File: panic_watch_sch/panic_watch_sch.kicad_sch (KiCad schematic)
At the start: 6 parts, among them IC1 STM32F401RET6, IC2 STM32F401RET6, IC3 STM32F401RET6

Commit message: Semi-finished schematic & config
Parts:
- added BT1: 9V, symbol Device:Battery_Cell
- added D2: IR204A, LED_THT:LED_D3.0mm_IRBlack, symbol LED:IR204A
- added DS2: WC1602A, Display:WC1602A, symbol Display_Character:WC1602A
- added IC4: STM32F401RET6, QFP50P1200X1200X160-64N, symbol STM32F401RET6:STM32F401RET6
- added LS1: Speaker, symbol Device:Speaker
- added PS1: ~, symbol STM32F401RET6:MB102
- added Q1: BC107, Package_TO_SOT_THT:TO-18-3, symbol Transistor_BJT:BC107
- added R1, R2, R3, R4, R5: 1k, symbol Device:R
- added SD1: ~, symbol STM32F401RET6:HW-203
- added U1, U2: TSSP58038, OptoDevice:Vishay_MINICAST-3Pin, symbol Sensor_Proximity:TSSP58038
- added U3: MAX98357A, Package_DFN_QFN:TQFN-16-1EP_3x3mm_P0.5mm_EP1.23x1.23mm, symbol Audio:MAX98357A
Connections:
- net at IC3.45 (PA12): now also U2.1 (OUT)
- net at IC3.47 (VSS_3): now also U2.2 (GND)
- net at IC3.48 (VDD_3): now also R2.2
- net at IC3.58 (PB6): now also IC2.58 (PB6), IC4.58 (PB6)
- net at IC3.59 (PB7): now also IC2.59 (PB7), IC4.57 (PB5)
- net at IC1.10 (PC2): now also DS1.9 (D2)
- net at IC1.11 (PC3): now also DS1.10 (D3)
- net at IC1.12 (VSSA/VREF-): now also U3.11 (GND), U3.15 (GND), U3.3 (GND)
- net Skin1: now reaches IC1.13 (VDDA/VREF+)
- net at IC1.18 (VSS_1): now also R4.1
- net at IC1.20 (PA4): now also U3.14 (LRCLK)
- net at IC1.22 (PA6): now also D1.3 (A), D2.2 (A)
- net at IC1.24 (PC4): now also DS1.11 (D4)
- net at IC1.25 (PC5): now also DS1.12 (D5)
- net at IC1.27 (PB1): now also Q1.1 (E)
- net at IC1.29 (PB10): now also SD1. (SCK)
- net at IC1.31 (VSS_2): now also SD1. (SCK)
- net at IC1.32 (VDD_2): now also SD1. (SCK)
- net at IC1.33 (PB12): now also SD1. (SCK)
- net Skin2: now reaches IC1.34 (PB13)
- net at IC1.35 (PB14): now also SD1. (SCK)
- net at IC1.36 (PB15): now also SD1. (SCK)
- net at IC1.37 (PC6): now also DS1.13 (D6)
- net at IC1.38 (PC7): now also DS1.14 (D7)
- net at IC1.39 (PC8): now also DS1.4 (RS)
- net at IC1.40 (PC9): now also DS1.5 (R/W)
- net at IC1.47 (VSS_3): now also MK1.1 (-)
- net at IC1.48 (VDD_3): now also R3.1
- net at IC1.50 (PA15): now also DS1.3 (VO)
- net at IC1.51 (PC10): now also U3.16 (BCLK)
- net at IC1.53 (PC12): now also U3.1 (DIN)
- net at IC1.54 (PD2): now also DS1.6 (E)
- net at IC1.63 (VSS_4): now also DS1.1 (VSS), DS1.16 (LED(-))
- net at IC1.64 (VDD_4): now also DS1.15 (LED(+))
- net at IC1.8 (PC0): now also DS1.7 (D0)
- net at IC1.9 (PC1): now also DS1.8 (D1)
- net +5V: now reaches DS1.2 (VDD)
- net +5V: now also DS2.2 (VDD), SD1. (SCK), U3.4 (~{SD_MODE}), U3.7 (VDD), U3.8 (VDD)
- net at D1.1 (BK): now also D2.1 (K), R4.2
- net at IC2.10 (PC2): now also DS2.9 (D2)
- net at IC2.11 (PC3): now also DS2.10 (D3)
- net at IC2.24 (PC4): now also DS2.11 (D4)
- net at IC2.25 (PC5): now also DS2.12 (D5)
- net at IC2.37 (PC6): now also DS2.13 (D6)
- net at IC2.38 (PC7): now also DS2.14 (D7)
- net at IC2.39 (PC8): now also DS2.4 (RS)
- net at IC2.40 (PC9): now also DS2.5 (R/W)
- net at IC2.50 (PA15): now also DS2.3 (VO)
- net at IC2.54 (PD2): now also DS2.6 (E)
- net at IC2.63 (VSS_4): now also DS2.1 (VSS), DS2.16 (LED(-))
- net at IC2.64 (VDD_4): now also DS2.15 (LED(+))
- net at IC2.8 (PC0): now also DS2.7 (D0)
- net at IC2.9 (PC1): now also DS2.8 (D1)
- net at MK1.2 (+): now also Q1.2 (B)
- new net: IC4.45 (PA12), U1.1 (OUT)
- new net: IC4.47 (VSS_3), U1.2 (GND)
- new net: R1.1, U1.3 (Vs)
- new net: Q1.3 (C), R3.2
- new net: R2.1, U2.3 (Vs)
- new net: R5.2, U3.2 (GAIN_SLOT)
- new net: IC4.48 (VDD_3), R1.2
- new net: LS1.1, U3.9 (OUTP)
- new net: LS1.2, U3.10 (OUTN)
- new net: BT1.1 (+), PS1. (Vout)
- new net: BT1.2 (-), PS1. (Vout)
- new net E5V: PS1. (Vout)
- new net GND: PS1. (Vout), R5.1
- no-connect marks 0 -> 1
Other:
- removed sheet Receiver and Bus
- removed sheet Wearable Accessory
- moved on the sheet: D1, DS1, IC1, IC2, IC3, MK1

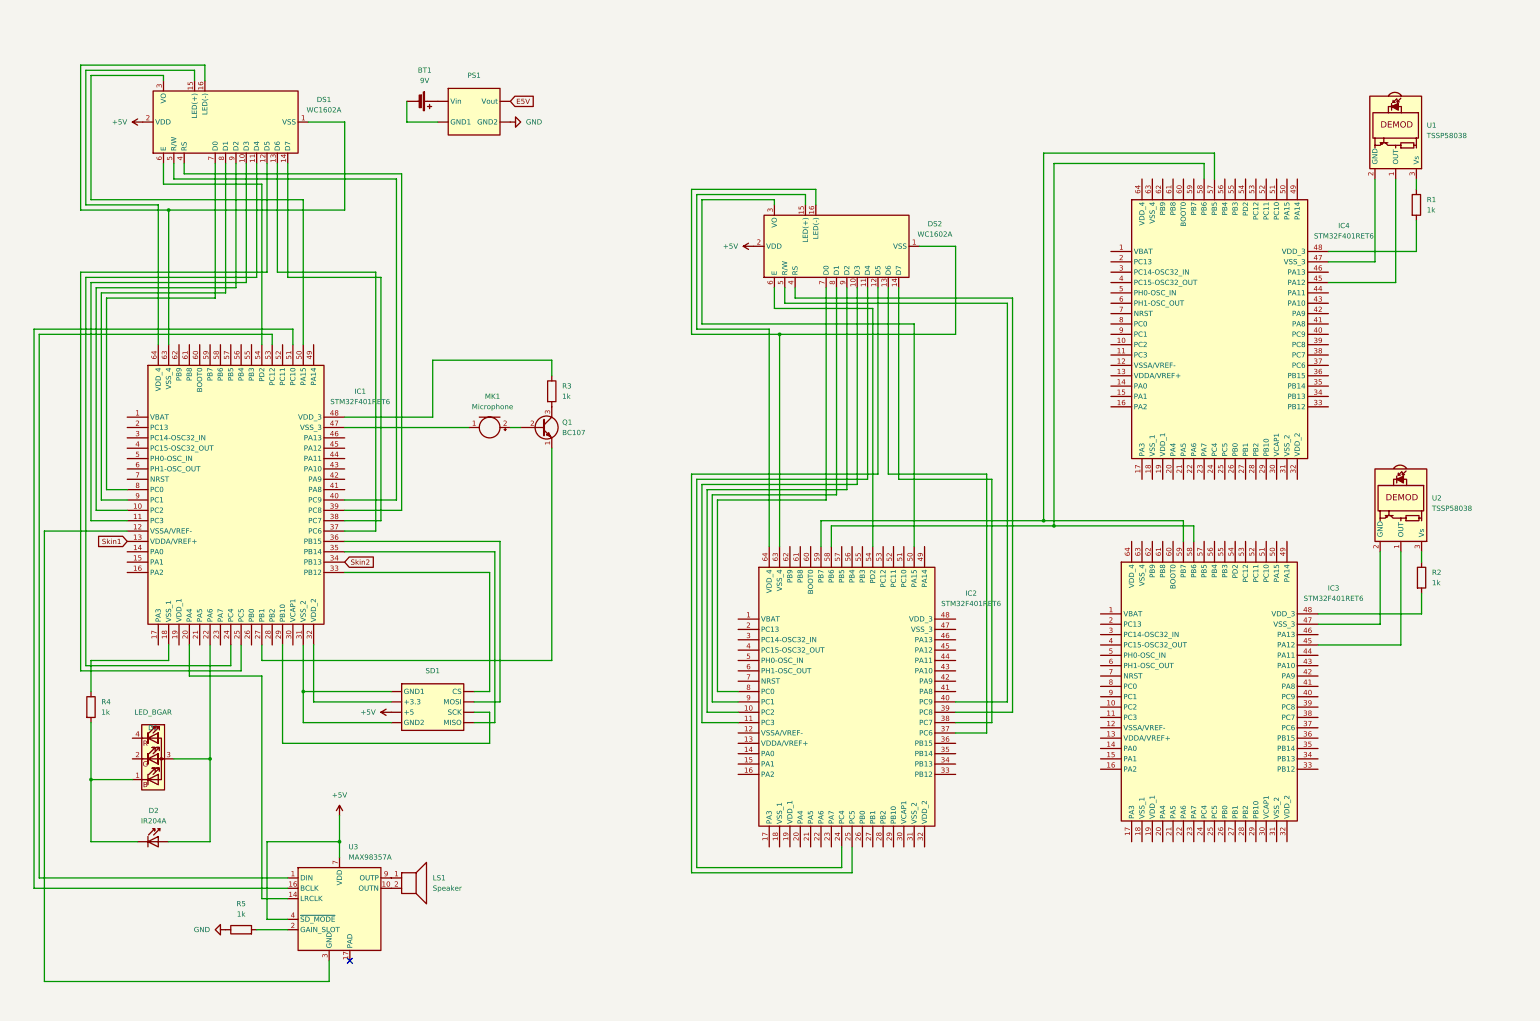
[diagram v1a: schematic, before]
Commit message: Blue LED working, tried my best to get sd card audio to work
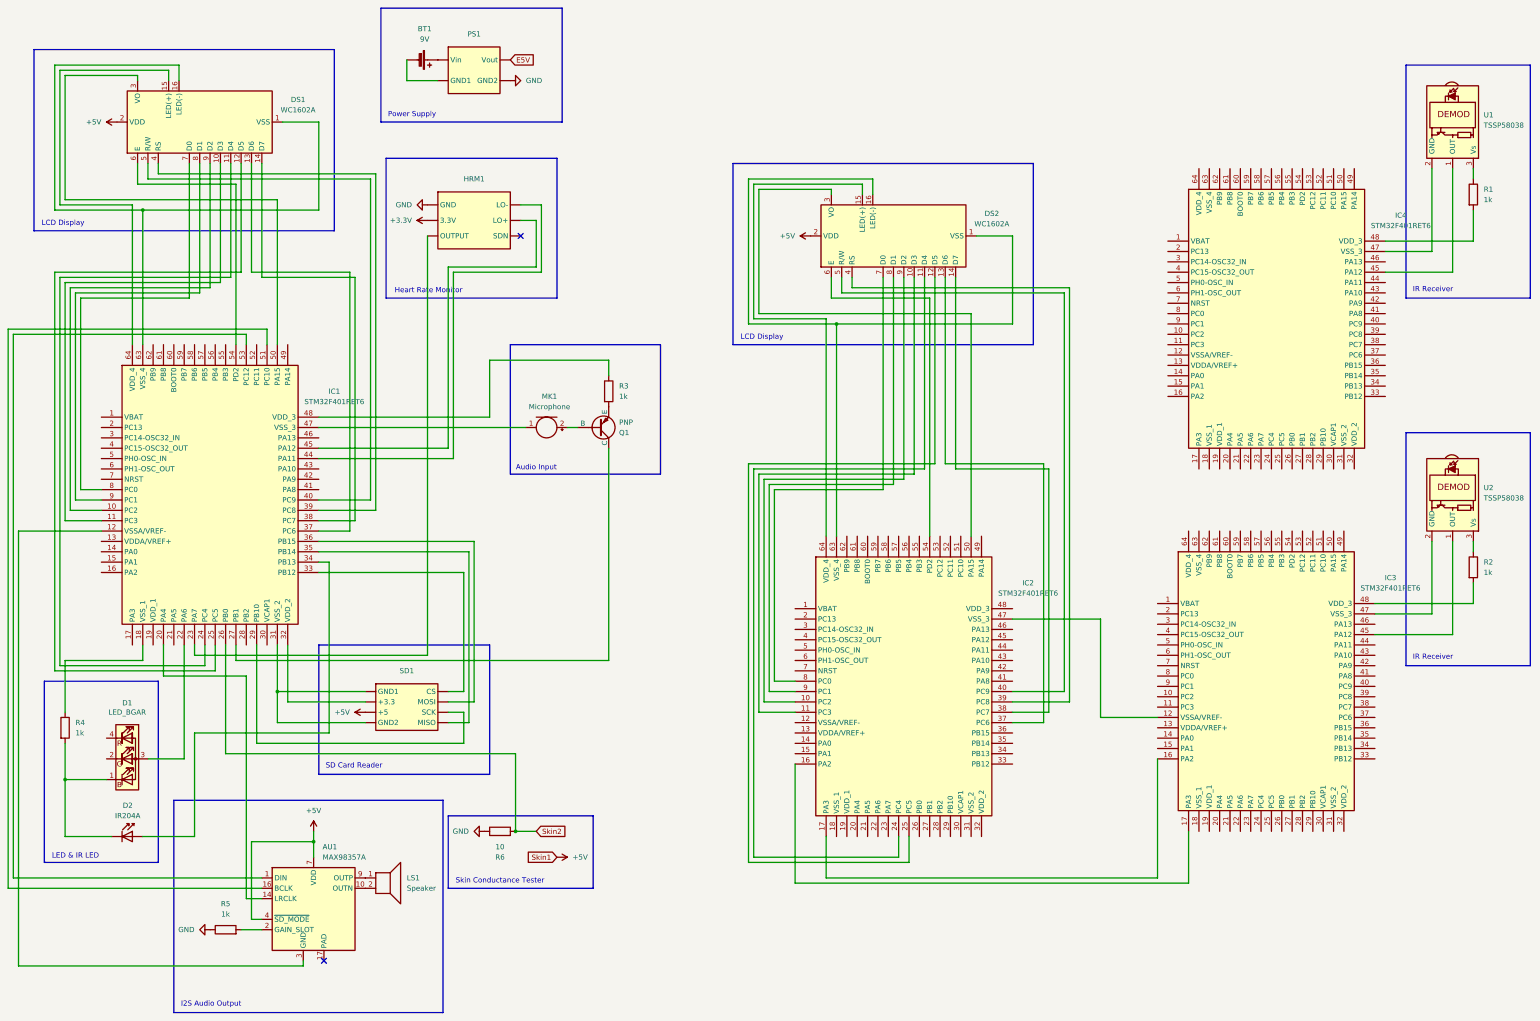
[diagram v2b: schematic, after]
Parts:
- removed Q1: BC107, Package_TO_SOT_THT:TO-18-3, symbol Transistor_BJT:BC107
- added HRM1: ~, symbol STM32F401RET6:AD8232
- added Q1: PNP, symbol Simulation_SPICE:PNP
- added R6: 10, symbol Device:R
- renumbered U3 to AU1
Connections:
- net GND: now also HRM1. (SDN), R6.1
- net Skin2: now also IC1.26 (PB0), R6.2; no longer IC1.34 (PB13)
- net at IC3.12 (VSSA/VREF-): now also IC2.47 (VSS_3)
- net at IC3.16 (PA2): now also IC2.17 (PA3)
- net at IC3.17 (PA3): now also IC2.16 (PA2)
- net at IC1.27 (PB1): now also Q1.1 (C)
- net at MK1.2 (+): now also Q1.2 (B)
- net at R3.2: now also Q1.3 (E)
- net at D1.3 (A), IC1.22 (PA6): no longer D2.2 (A)
- net at IC1.23 (PA7): now also HRM1. (SDN)
- net at IC1.44 (PA11): now also HRM1. (SDN)
- net at IC1.45 (PA12): now also HRM1. (SDN)
- net Skin1: no longer names the net of IC1.13 (VDDA/VREF+)
- new net: D2.2 (A), IC1.34 (PB13)
- new net +3.3V: HRM1. (SDN)
- now unconnected: IC2.58 (PB6), IC2.59 (PB7), IC3.58 (PB6), IC3.59 (PB7), IC4.57 (PB5), IC4.58 (PB6)
- no-connect marks 1 -> 2
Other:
- note added: "Audio Input"
- note added: "Heart Rate Monitor"
- note added: "I2S Audio Output"
- note added: "IR Receiver"
- note added: "LCD Display"
- note added: "LED & IR LED"
- note added: "Power Supply"
- note added: "SD Card Reader"
- note added: "Skin Conductance Tester"
- moved on the sheet: AU1, BT1, D1, D2, DS1, DS2, IC1, IC2, IC3, IC4, LS1, MK1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

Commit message: Add motivational messages, change sch, change fft duration
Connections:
- net at IC3.16 (PA2): no longer IC2.17 (PA3)
- net at IC3.17 (PA3): no longer IC2.16 (PA2)
- net at IC3.37 (PC6): now also IC2.45 (PA12)
- net at IC3.38 (PC7): now also IC2.44 (PA11)
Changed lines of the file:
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@@
-	(wire
-		(pts
-			(xy 224.79 207.01) (xy 224.79 236.22)
-		)
-		(stroke
-			(width 0)
-			(type default)
-		)
-	)
 	(wire
 		(pts
@@
 	(wire
 		(pts
+			(xy 374.65 229.87) (xy 294.64 229.87)
+		)
+		(stroke
+			(width 0)
+			(type default)
+		)
+	)
+	(wire
+		(pts
 			(xy 95.25 100.33) (xy 31.75 100.33)
 		)
@@
 	(wire
 		(pts
+			(xy 367.03 193.04) (xy 374.65 193.04)
+		)
+		(stroke
+			(width 0)
+			(type default)
+		)
+	)
+	(wire
+		(pts
 			(xy 238.76 90.17) (xy 292.1 90.17)
 		)
@@
 	(wire
 		(pts
+			(xy 295.91 228.6) (xy 373.38 228.6)
+		)
+		(stroke
+			(width 0)
+			(type default)
+		)
+	)
+	(wire
+		(pts
 			(xy 107.95 154.94) (xy 144.78 154.94)
 		)
@@
 	(wire
 		(pts
+			(xy 295.91 176.53) (xy 295.91 228.6)
+		)
+		(stroke
+			(width 0)
+			(type default)
+		)
+	)
+	(wire
+		(pts
 			(xy 259.08 87.63) (xy 259.08 133.35)
 		)
@@
 	(wire
 		(pts
+			(xy 373.38 195.58) (xy 367.03 195.58)
+		)
+		(stroke
+			(width 0)
+			(type default)
+		)
+	)
+	(wire
+		(pts
 			(xy 219.71 186.69) (xy 224.79 186.69)
 		)
@@
 	(wire
 		(pts
+			(xy 278.13 176.53) (xy 295.91 176.53)
+		)
+		(stroke
+			(width 0)
+			(type default)
+		)
+	)
+	(wire
+		(pts
 			(xy 256.54 134.62) (xy 214.63 134.62)
 		)
@@
 	(wire
 		(pts
-			(xy 321.31 236.22) (xy 321.31 223.52)
-		)
-		(stroke
-			(width 0)
-			(type default)
-		)
-	)
-	(wire
-		(pts
 			(xy 64.77 71.12) (xy 107.95 71.12)
 		)
@@
 	(wire
 		(pts
-			(xy 232.41 234.95) (xy 232.41 224.79)
+			(xy 374.65 193.04) (xy 374.65 229.87)
 		)
 		(stroke
@@
 	(wire
 		(pts
-			(xy 313.69 205.74) (xy 313.69 234.95)
-		)
-		(stroke
-			(width 0)
-			(type default)
-		)
-	)
-	(wire
-		(pts
 			(xy 46.99 144.78) (xy 54.61 144.78)
 		)
@@
 	(wire
 		(pts
-			(xy 313.69 234.95) (xy 232.41 234.95)
-		)
-		(stroke
-			(width 0)
-			(type default)
-		)
-	)
-	(wire
-		(pts
 			(xy 213.36 99.06) (xy 213.36 63.5)
 		)
@@
 	(wire
 		(pts
-			(xy 224.79 236.22) (xy 321.31 236.22)
-		)
-		(stroke
-			(width 0)
-			(type default)
-		)
-	)
-	(wire
-		(pts
 			(xy 215.9 194.31) (xy 224.79 194.31)
 		)
@@
 	(wire
 		(pts
+			(xy 373.38 228.6) (xy 373.38 195.58)
+		)
+		(stroke
+			(width 0)
+			(type default)
+		)
+	)
+	(wire
+		(pts
 			(xy 217.17 137.16) (xy 217.17 191.77)
 		)
@@
 	(wire
 		(pts
+			(xy 294.64 179.07) (xy 278.13 179.07)
+		)
+		(stroke
+			(width 0)
+			(type default)
+		)
+	)
+	(wire
+		(pts
 			(xy 76.2 59.69) (xy 76.2 92.71)
 		)
@@
 		)
 		(stroke
+			(width 0)
+			(type default)
+		)
+	)
+	(wire
+		(pts
+			(xy 294.64 229.87) (xy 294.64 179.07)
+		)
+		(stroke

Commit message: previous schematic changes, more tutorial citations
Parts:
- removed BT1: 9V, symbol Device:Battery_Cell
- removed IC3, IC4: STM32F401RET6, QFP50P1200X1200X160-64N, symbol STM32F401RET6:STM32F401RET6
- removed MK1: Microphone, symbol Device:Microphone
- removed PS1: ~, symbol STM32F401RET6:MB102
- removed Q1: PNP, symbol Simulation_SPICE:PNP
- removed R1, R2, R3: 1k, symbol Device:R
- removed U1, U2: TSSP58038, OptoDevice:Vishay_MINICAST-3Pin, symbol Sensor_Proximity:TSSP58038
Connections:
- net at IC2.47 (VSS_3): now also IC1.47 (VSS_3)
- net at IC2.45 (PA12): now also IC1.42 (PA9)
- net at IC2.44 (PA11): now also IC1.43 (PA10)
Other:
- note removed: "Audio Input"
- note removed: "IR Receiver"
- note removed: "Power Supply"
